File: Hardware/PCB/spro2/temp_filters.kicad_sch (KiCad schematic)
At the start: 7 parts, among them U3 OPA340P

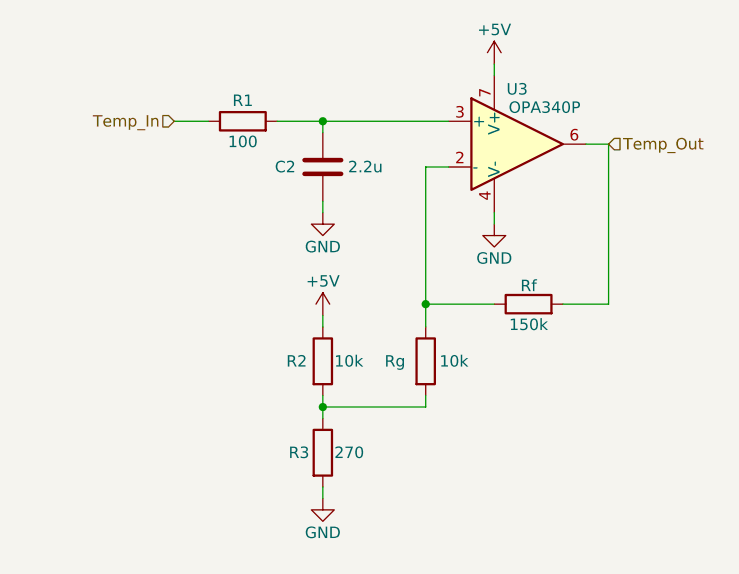
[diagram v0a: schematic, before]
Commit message: Updated circuit
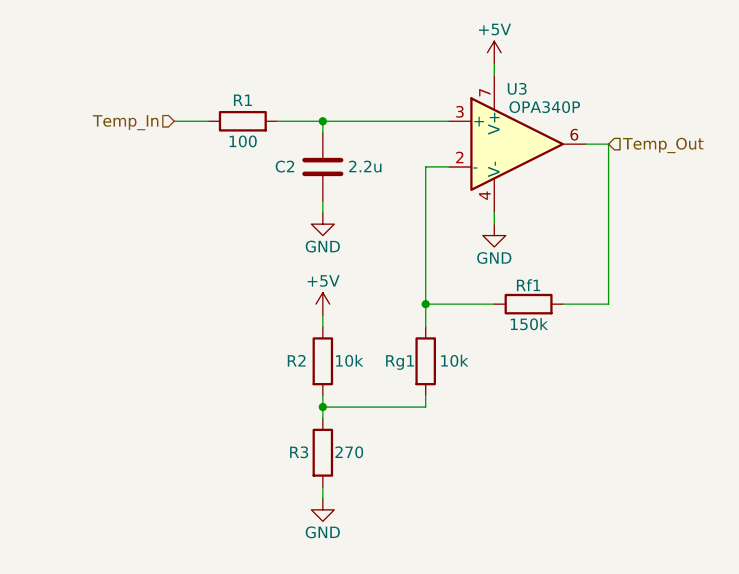
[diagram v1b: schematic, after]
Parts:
- renumbered Rf to Rf1, Rg to Rg1
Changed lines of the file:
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@@
 		(on_board yes)
 		(dnp no)
-		(property "Reference" "#PWR011"
+		(property "Reference" "#PWR014"
 			(at 115.57 39.37 0)
 			(effects
@@
 		(pin "1"
 		)
+		(instances
+			(project "spro2"
+				(path "/edfea366-2226-45cc-893f-1155e0ffe333/1ed492d3-a3aa-4e29-adfa-514232caea13"
+					(reference "#PWR014")
+					(unit 1)
+				)
+			)
+		)
 	)
 	(symbol
@@
 		(on_board yes)
 		(dnp no)
-		(property "Reference" "#PWR03"
+		(property "Reference" "#PWR013"
 			(at 96.52 90.17 0)
 			(effects
@@
 			(project "spro2"
 				(path "/edfea366-2226-45cc-893f-1155e0ffe333/1ed492d3-a3aa-4e29-adfa-514232caea13"
-					(reference "#PWR03")
+					(reference "#PWR013")
 					(unit 1)
 				)
@@
 		(on_board yes)
 		(dnp no)
-		(property "Reference" "#PWR012"
+		(property "Reference" "#PWR015"
 			(at 115.57 59.69 0)
 			(effects
@@
 		(pin "1"
 		)
+		(instances
+			(project "spro2"
+				(path "/edfea366-2226-45cc-893f-1155e0ffe333/1ed492d3-a3aa-4e29-adfa-514232caea13"
+					(reference "#PWR015")
+					(unit 1)
+				)
+			)
+		)
 	)
 	(symbol
@@
 		(on_board yes)
 		(dnp no)
-		(property "Reference" "Rf"
+		(property "Reference" "Rf1"
 			(at 119.38 60.198 90)
 			(effects
@@
 			(project ""
 				(path "/edfea366-2226-45cc-893f-1155e0ffe333/1ed492d3-a3aa-4e29-adfa-514232caea13"
-					(reference "Rf")
+					(reference "Rf1")
 					(unit 1)
 				)
@@
 		(on_board yes)
 		(dnp no)
-		(property "Reference" "#PWR04"
+		(property "Reference" "#PWR012"
 			(at 96.52 67.31 0)
 			(effects
@@
 			(project "spro2"
 				(path "/edfea366-2226-45cc-893f-1155e0ffe333/1ed492d3-a3aa-4e29-adfa-514232caea13"
-					(reference "#PWR04")
+					(reference "#PWR012")
 					(unit 1)
 				)
@@
 		(on_board yes)
 		(dnp no)
-		(property "Reference" "#PWR01"
+		(property "Reference" "#PWR011"
 			(at 96.52 58.42 0)
 			(effects
@@
 			(project "spro2"
 				(path "/edfea366-2226-45cc-893f-1155e0ffe333/1ed492d3-a3aa-4e29-adfa-514232caea13"
-					(reference "#PWR01")
+					(reference "#PWR011")
 					(unit 1)
 				)
@@
 		(on_board yes)
 		(dnp no)
-		(property "Reference" "Rg"
+		(property "Reference" "Rg1"
 			(at 103.378 68.58 0)
 			(effects
@@
 			(project ""
 				(path "/edfea366-2226-45cc-893f-1155e0ffe333/1ed492d3-a3aa-4e29-adfa-514232caea13"
-					(reference "Rg")
+					(reference "Rg1")
 					(unit 1)
 				)
@@
 		(pin "2"
 		)
-	)
+		(instances
+			(project "spro2"
+				(path "/edfea366-2226-45cc-893f-1155e0ffe333/1ed492d3-a3aa-4e29-adfa-514232caea13"
+					(reference "U3")
+					(unit 1)
+				)
+			)
+		)
+	)

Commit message: Updated schematic and 1st version of the PCB
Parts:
- C2: footprint (none) -> Capacitor_THT:CP_Radial_D5.0mm_P2.00mm
- R1, R2, R3, Rf1, Rg1: footprint (none) -> Resistor_THT:R_Axial_DIN0207_L6.3mm_D2.5mm_P10.16mm_Horizontal
- renumbered U3 to U2
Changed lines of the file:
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@@
 			)
 		)
-		(property "Footprint" ""
+		(property "Footprint" "Resistor_THT:R_Axial_DIN0207_L6.3mm_D2.5mm_P10.16mm_Horizontal"
 			(at 94.742 78.74 90)
 			(effects
@@
 			)
 		)
-		(property "Footprint" ""
+		(property "Footprint" "Capacitor_THT:CP_Radial_D5.0mm_P2.00mm"
 			(at 97.4852 50.8 0)
 			(effects
@@
 			)
 		)
-		(property "Footprint" ""
+		(property "Footprint" "Resistor_THT:R_Axial_DIN0207_L6.3mm_D2.5mm_P10.16mm_Horizontal"
 			(at 119.38 64.008 90)
 			(effects
@@
 			)
 		)
-		(property "Footprint" ""
+		(property "Footprint" "Resistor_THT:R_Axial_DIN0207_L6.3mm_D2.5mm_P10.16mm_Horizontal"
 			(at 94.742 68.58 90)
 			(effects
@@
 			)
 		)
-		(property "Footprint" ""
+		(property "Footprint" "Resistor_THT:R_Axial_DIN0207_L6.3mm_D2.5mm_P10.16mm_Horizontal"
 			(at 87.63 43.688 90)
 			(effects
@@
 			)
 		)
-		(property "Footprint" ""
+		(property "Footprint" "Resistor_THT:R_Axial_DIN0207_L6.3mm_D2.5mm_P10.16mm_Horizontal"
 			(at 106.172 68.58 90)
 			(effects
@@
 		(on_board yes)
 		(dnp no)
-		(property "Reference" "U3"
+		(property "Reference" "U2"
 			(at 118.11 38.354 0)
 			(effects
@@
 			(project "spro2"
 				(path "/edfea366-2226-45cc-893f-1155e0ffe333/1ed492d3-a3aa-4e29-adfa-514232caea13"
-					(reference "U3")
-					(unit 1)
-				)
+					(reference "U2")
+					(unit 1)
+				)

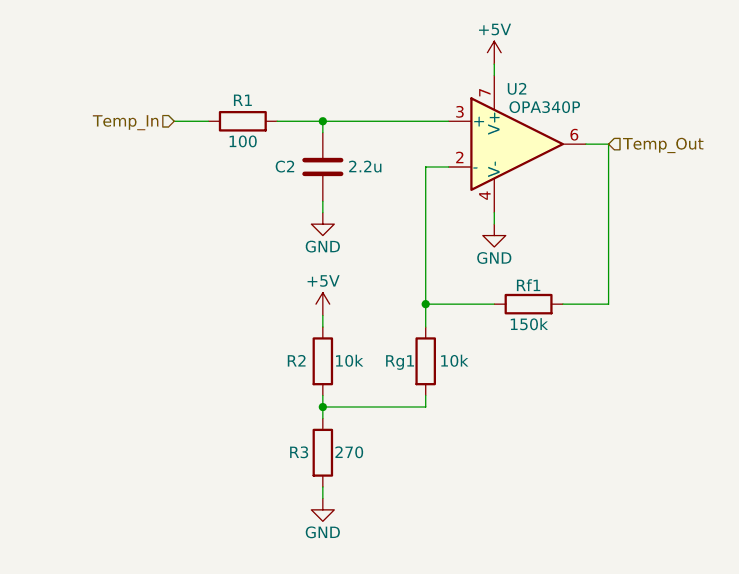
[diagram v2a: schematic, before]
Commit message: Temp circ fixed, added footprint for MAX6
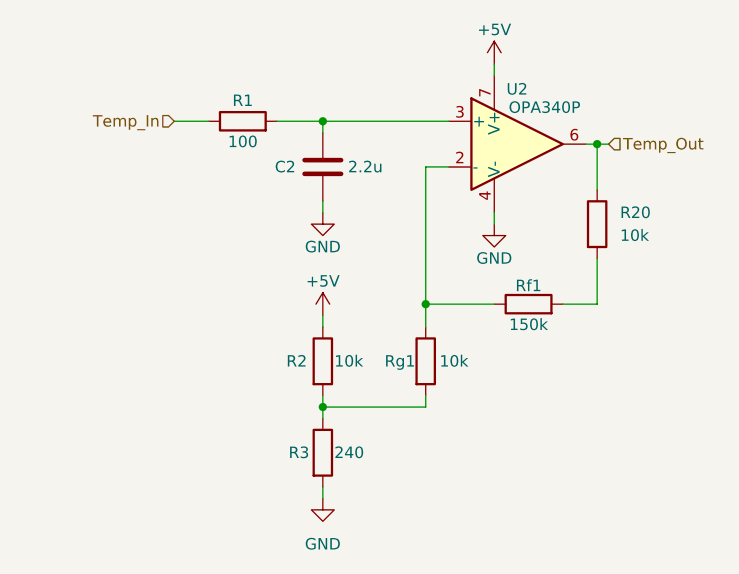
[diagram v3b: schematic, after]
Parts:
- added R20: 10k, symbol Device:R
- R3: value 270 -> 240
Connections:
- net Temp_Out: now also R20.1; no longer Rf1.2
- new net: R20.2, Rf1.2

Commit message: Hopefully last version of PCB
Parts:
- removed C2: 2.2u, Capacitor_THT:CP_Radial_D5.0mm_P2.00mm, symbol Device:C
- added C6: 2.2u, Capacitor_THT:CP_Radial_D6.3mm_P2.50mm, symbol Device:C_Polarized
- R4: renamed from R20; footprint (none) -> Resistor_THT:R_Axial_DIN0207_L6.3mm_D2.5mm_P10.16mm_Horizontal
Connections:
- net GND: now also C6.2
- net at R1.2, U2.3 (+): now also C6.1

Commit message: Final scheamtic mega trust
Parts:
- R1: value 100 -> 1.5k
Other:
- moved on the sheet: C6, R1
